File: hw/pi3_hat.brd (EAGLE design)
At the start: 56.5 x 65 mm, 110 parts, among them J1 XT30P, J2 XT30P, U1 AP64351SO8EP, U10 CAT24C32SOIC8, U11 STM32G474CEU6, U12 TCAN334GSOT23, U13 TCAN334GSOT23, U2 DMMT5401, U3 DMG2305UX, U4 STM32G474CEU6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

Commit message: Select parts
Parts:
- C6: value 3.3nF -> 4.7nF
- R1: value 14k -> 15k
- R15, R16: value 3.9k 1% -> 4.7k
- R4: value ~700 -> 560
- moved +5V 2.91 mm to (7.90, 3.10)
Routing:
- net +5V: track 19.9 -> 18.9 mm

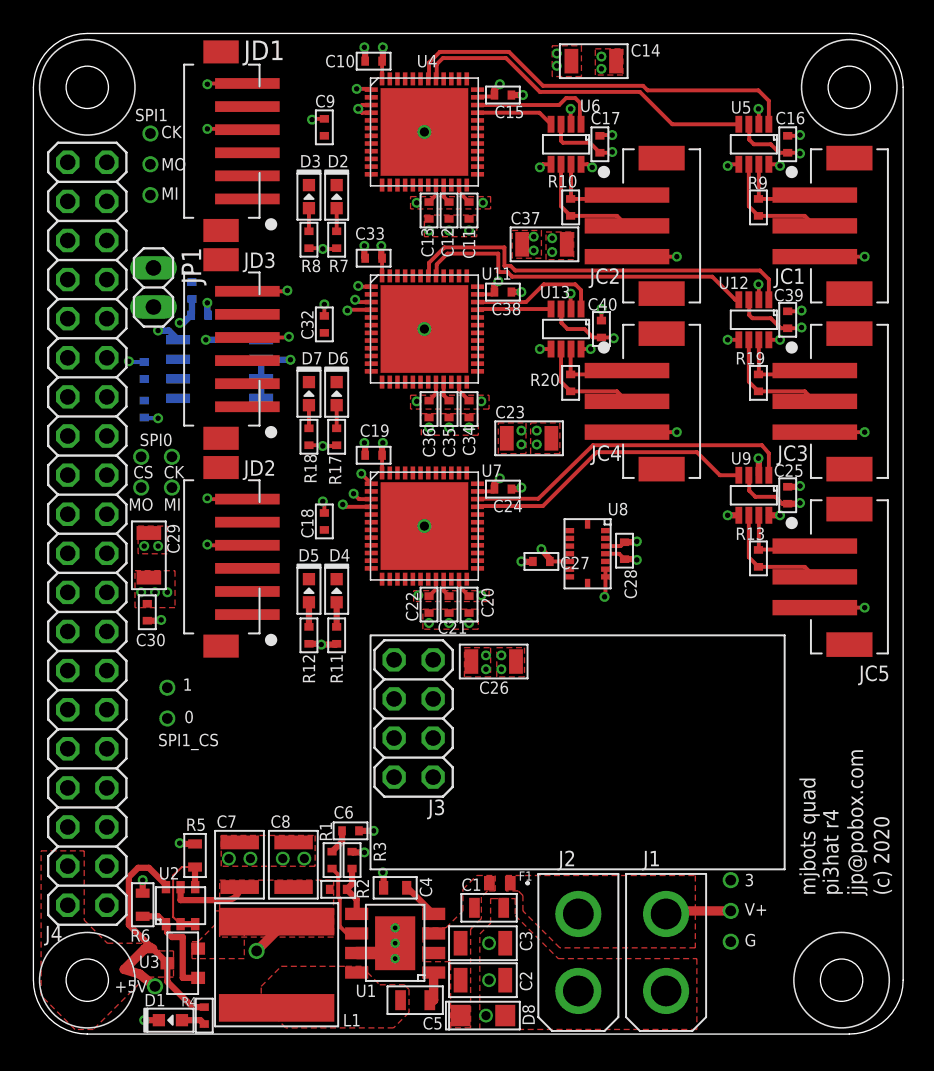
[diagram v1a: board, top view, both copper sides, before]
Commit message: Minor silk tweaks, re-autoroute with bottom layer up/down
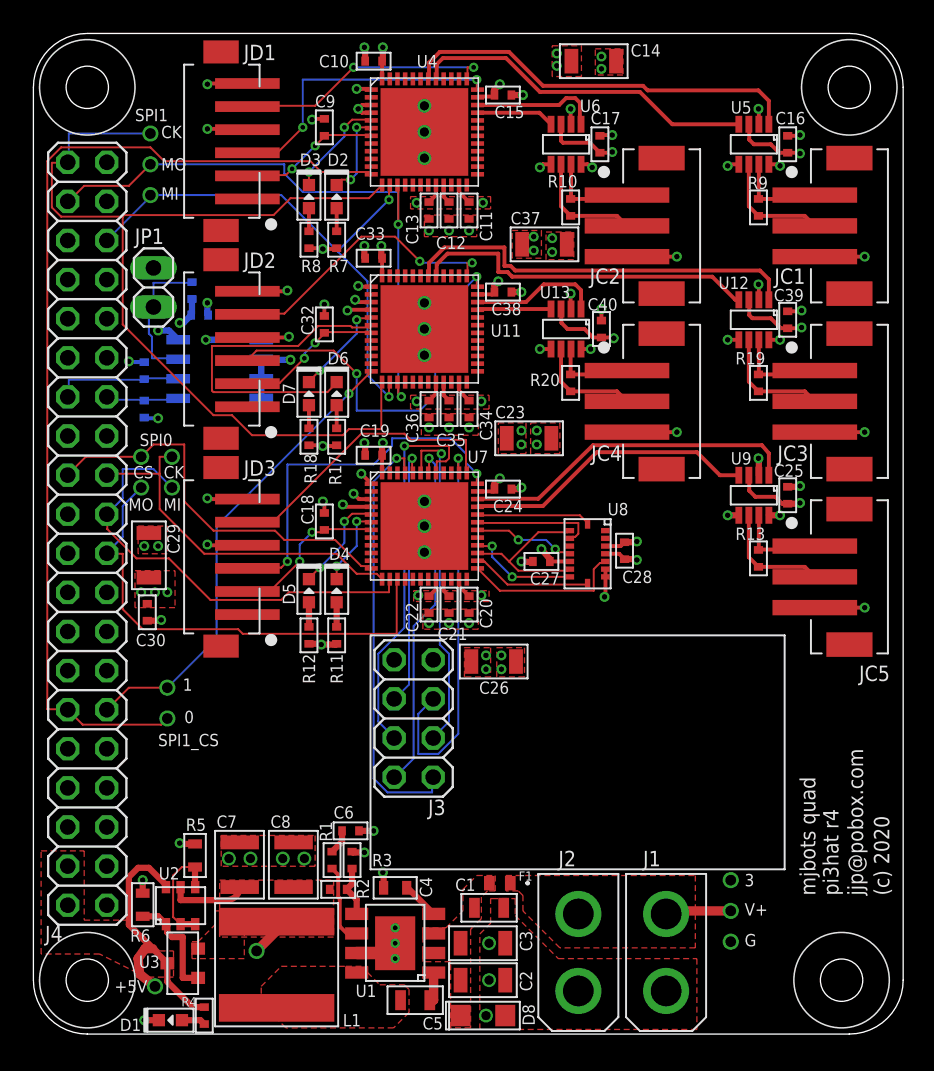
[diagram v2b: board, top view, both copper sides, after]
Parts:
- moved JD2 13.5 mm to (11.9, 44.5)
- moved JD3 13.5 mm to (11.9, 31.0)
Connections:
- new net PI_RX_3V: J4.10
- net N$32: now also JD2.2; no longer JD3.2
- net N$33: now also JD2.3; no longer JD3.3
- net N$34: now also JD2.5; no longer JD3.5
- net N$47: now also JD3.2; no longer JD2.2
- net N$48: now also JD3.3; no longer JD2.3
- net N$49: now also JD3.5; no longer JD2.5
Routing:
- net SPI1_CS0: track 0.00 -> 66.1 mm
- net SPI1_SCLK: track 0.00 -> 63.7 mm
- net SPI1_MOSI: track 0.00 -> 40.7 mm, vias 0 -> 2
- net SPI1_MISO: track 0.00 -> 35.3 mm, vias 0 -> 2
- net SPI0_MOSI: track 0.00 -> 31.9 mm
- net SPI1_CS1: track 0.00 -> 30.6 mm, vias 0 -> 1
- net SPI0_MISO: track 0.00 -> 29.3 mm
- net NRF_IRQ: track 0.00 -> 28.1 mm, vias 0 -> 1
- net SPI0_CS0: track 0.00 -> 26.1 mm
- net NRF_CS: track 0.00 -> 26.0 mm, vias 0 -> 1
- net NRF_SCK: track 0.00 -> 25.4 mm, vias 0 -> 1
- net N$33: track 0.00 -> 25.4 mm, vias 0 -> 2
- net N$48: track 0.00 -> 24.4 mm, vias 0 -> 2
- net SPI0_SCLK: track 0.00 -> 24.0 mm
- net NRF_MISO: track 0.00 -> 23.0 mm, vias 0 -> 1
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
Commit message: Basic SPI slave operation that works at least a little
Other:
- board text added: "mjbots quad pi3hat r4.1"
- board text removed: "mjbots quad pi3hat r4"
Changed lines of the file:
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@@
 <text x="55.6" y="9" size="1" layer="21" ratio="10" rot="R90">(c) 2020</text>
 <text x="52.3" y="9" size="1" layer="21" ratio="10" rot="R90">mjbots quad
-pi3hat r4</text>
+pi3hat r4.1</text>
 <wire x1="21.95" y1="25.9" x2="48.8" y2="25.9" width="0.127" layer="21"/>
 <wire x1="48.8" y1="25.9" x2="48.8" y2="10.7" width="0.127" layer="21"/>
@@
 </element>
 <element name="U1" library="pi3_hat" package="SO-8EP" value="AP64351SO8EP" x="23.5" y="5.9" smashed="yes" rot="R90">
-<attribute name="MPN" value="AP64350SP-13" x="23.5" y="5.9" size="1.778" layer="27" rot="R90" display="off"/>
+<attribute name="MPN" value="AP64351SP-13" x="23.5" y="5.9" size="1.778" layer="27" rot="R90" display="off"/>
 <attribute name="POPULATE" value="1" x="23.5" y="5.9" size="1.778" layer="27" rot="R90" display="off"/>
 <attribute name="MF" value="DIODES INC" x="23.5" y="5.9" size="1.778" layer="27" rot="R90" display="off"/>

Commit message: Add mjbots logo
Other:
- board text added: "pi3hat r4.2"
- board text removed: "jjp@pobox.com"
- board text removed: "mjbots quad pi3hat r4.1"

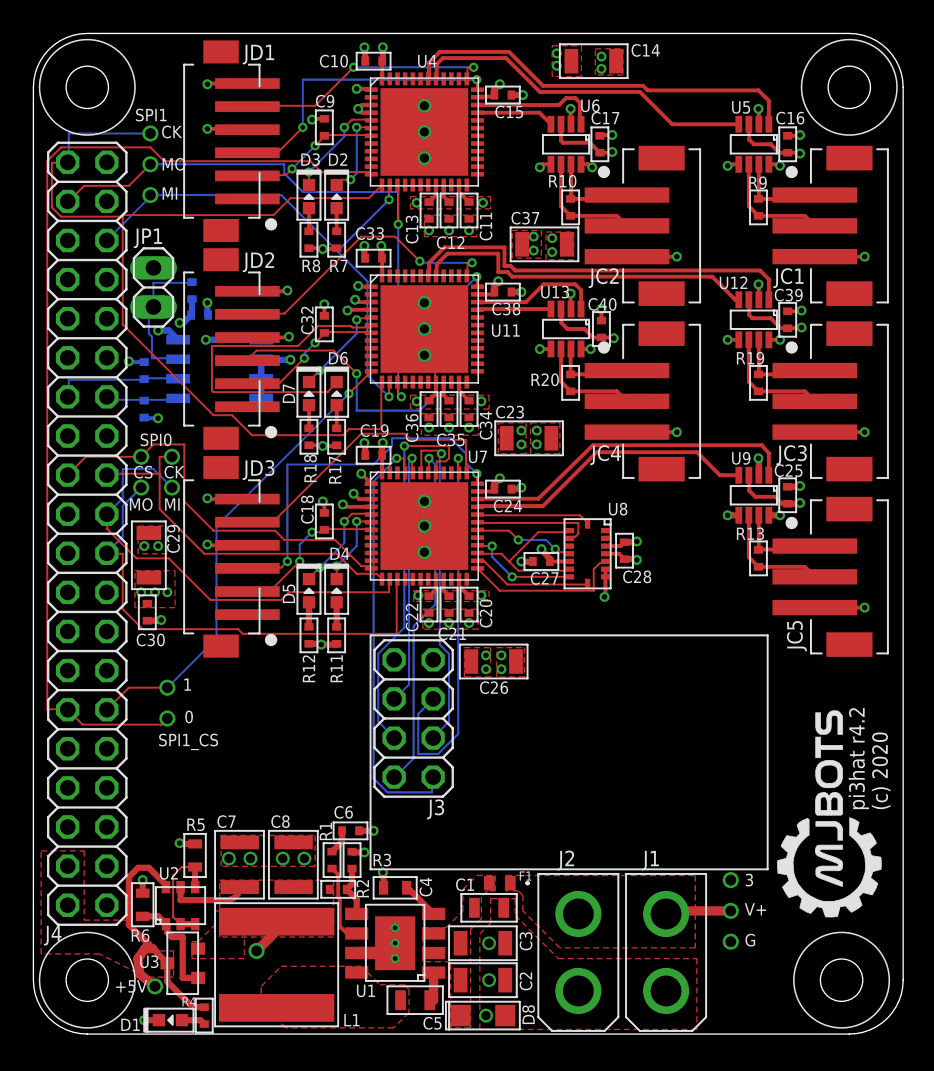
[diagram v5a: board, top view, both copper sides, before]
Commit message: Add debug pads for each processor
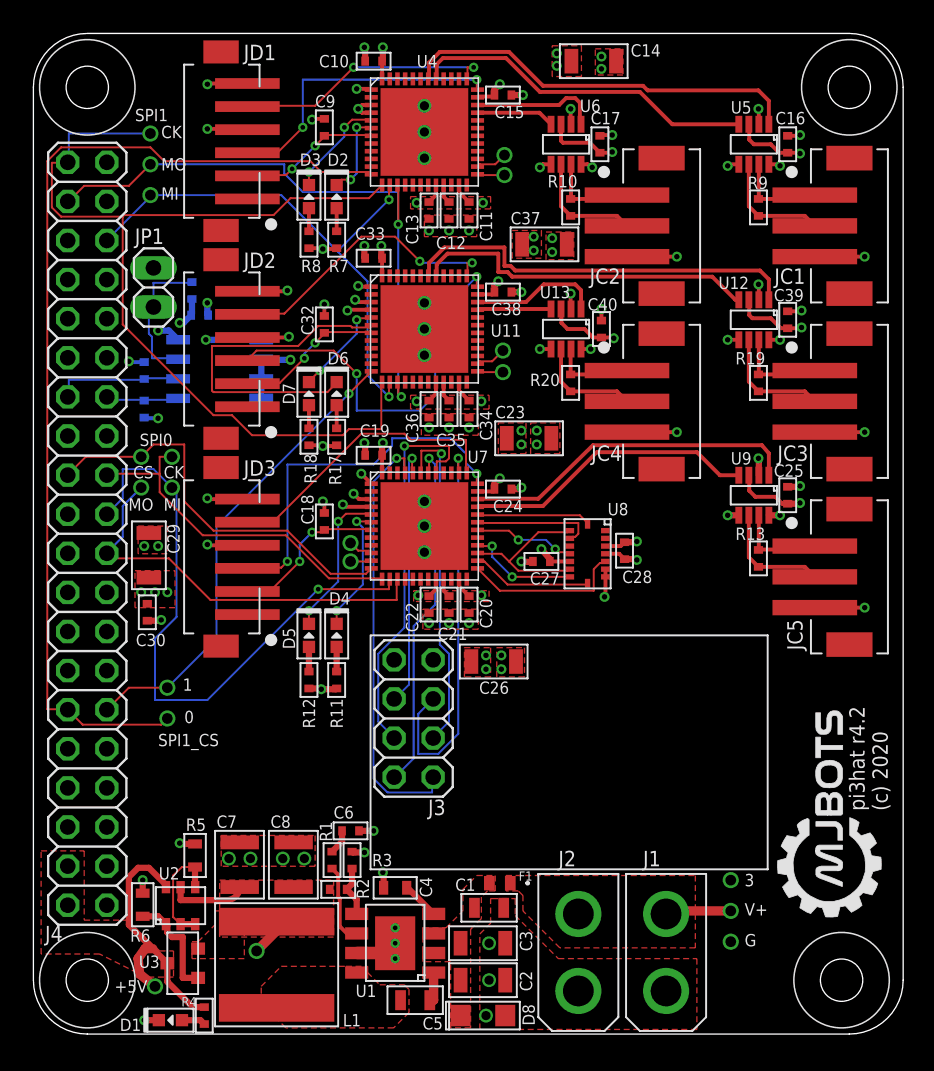
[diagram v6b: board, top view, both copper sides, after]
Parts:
- added DBG1A, DBG1B, DBG2A, DBG2B, DBG3A, DBG3B: PAD24AWG_PAD, pi3_hat:24AWG_PAD
- moved D4 2.90 mm to (19.7, 25.9)
- moved D5 2.90 mm to (17.9, 25.9)
- moved R11 2.90 mm to (19.7, 23.0)
- moved R12 2.90 mm to (17.9, 23.0)
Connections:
- new net DBG1A: DBG1A.P$1, U4.26
- new net DBG1B: DBG1B.P$1, U4.25
- new net DBG2A: DBG2A.P$1, U11.26
- new net DBG2B: DBG2B.P$1, U11.25
- new net DBG3A: DBG3A.P$1, U7.10
- new net DBG3B: DBG3B.P$1, U7.11
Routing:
- net SPI0_MISO: track 29.3 -> 40.4 mm, vias 0 -> 1
- net SPI0_MOSI: track 31.9 -> 26.6 mm
- net N$53: track 5.26 -> 8.49 mm
- net N$51: track 6.68 -> 9.81 mm
- net DBG1A: track 0.00 -> 2.06 mm
- net DBG2A: track 0.00 -> 2.00 mm
- net DBG1B: track 0.00 -> 1.77 mm
- net DBG2B: track 0.00 -> 1.67 mm
- net DBG3A: track 0.00 -> 1.62 mm
- net DBG3B: track 0.00 -> 1.37 mm
- net SPI0_SCLK: track 24.0 -> 23.4 mm

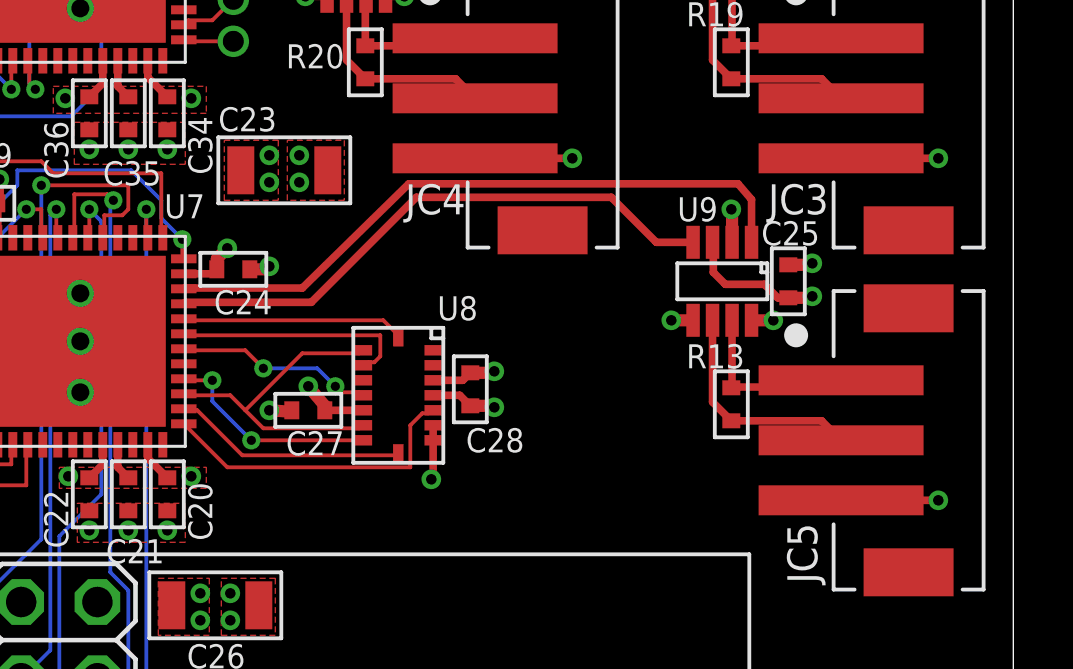
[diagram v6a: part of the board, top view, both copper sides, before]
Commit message: Switch the aux CAN to the LTC2875
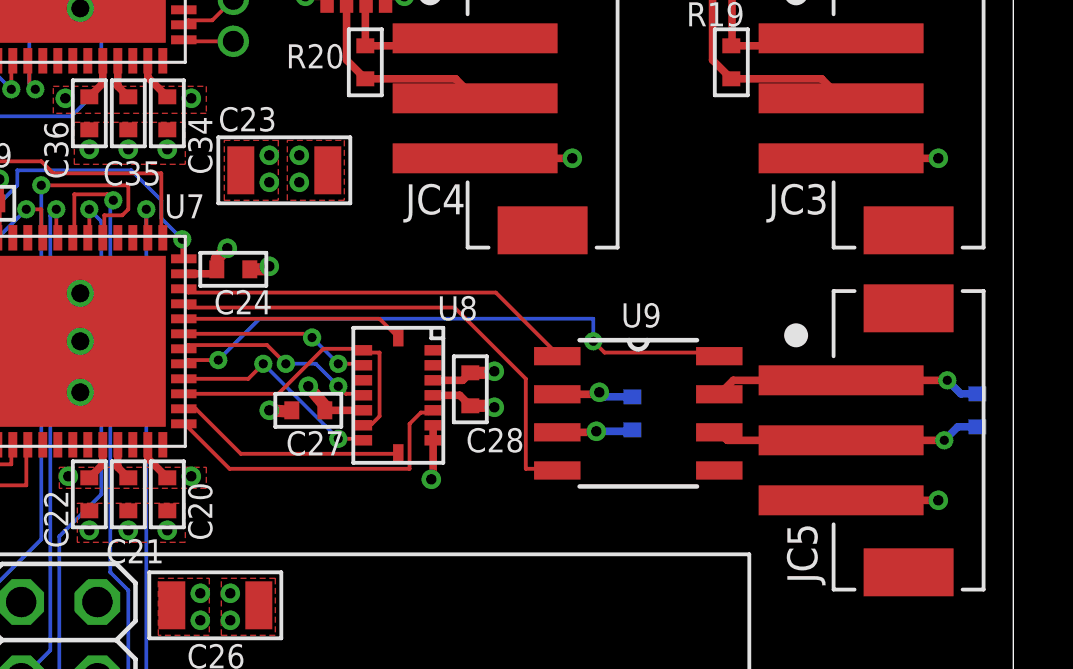
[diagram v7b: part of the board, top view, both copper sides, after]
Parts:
- U9: value TCAN334GSOT23 -> LTC2875; device pi3_hat:SOT23-8 -> pi3_hat:SOIC8
- moved R13 8.20 mm to (55.3, 30.7), flipped to the bottom
- moved C25 6.81 mm to (43.8, 30.6), flipped to the bottom
- moved U9 5.22 mm to (44.0, 30.6), turned to 0 degrees
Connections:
- new net CAN_SHDN: U7.29, U9.8
- net GND: no longer U9.5, U9.8
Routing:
- net CAN_SHDN: track 0.00 -> 19.4 mm, vias 0 -> 2
- net N$55: track 22.0 -> 13.4 mm
- net N$45: track 5.99 -> 9.30 mm, vias 0 -> 1
- net N$54: track 19.1 -> 16.5 mm
- net +3V3: track 76.7 -> 74.6 mm
- net IMU_CS1: track 7.95 -> 6.42 mm, vias 0 -> 2
- net N$46: track 7.54 -> 8.90 mm, vias 0 -> 1
- net IMU_MISO: track 11.3 -> 10.00 mm
- net GND: track 76.1 -> 75.3 mm, vias 88 -> 85

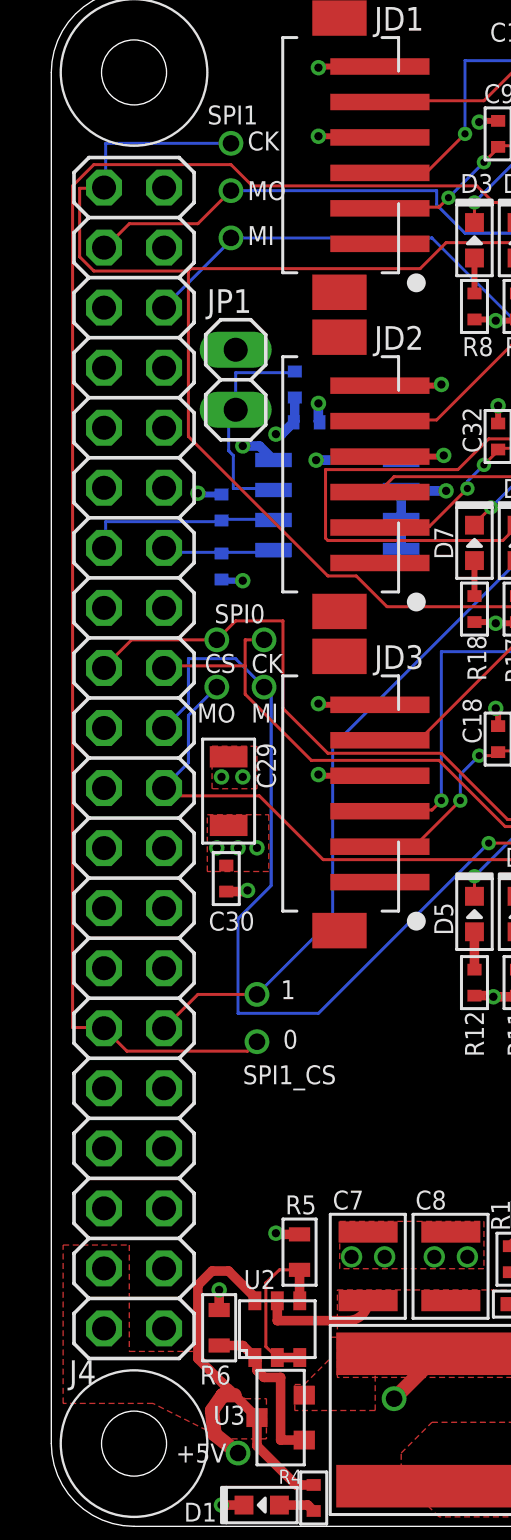
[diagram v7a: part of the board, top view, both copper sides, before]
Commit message: Flip rpi header start populating it, stop populating NRF header
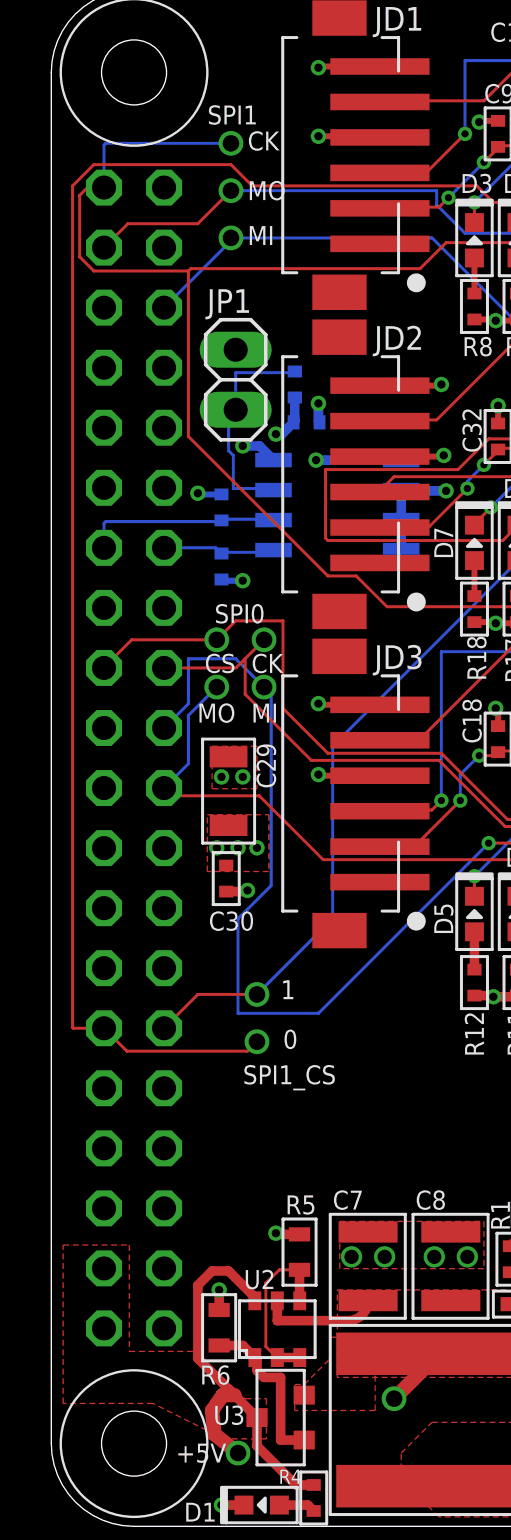
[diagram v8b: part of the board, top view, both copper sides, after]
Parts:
- J4: device pinhead:2X20 -> pi3_hat:2X20FLIP
- flipped J4 to the bottom
